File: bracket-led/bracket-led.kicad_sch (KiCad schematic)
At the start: 1 part, among them J1 BM08B-SURS-TF(LF)(SN)

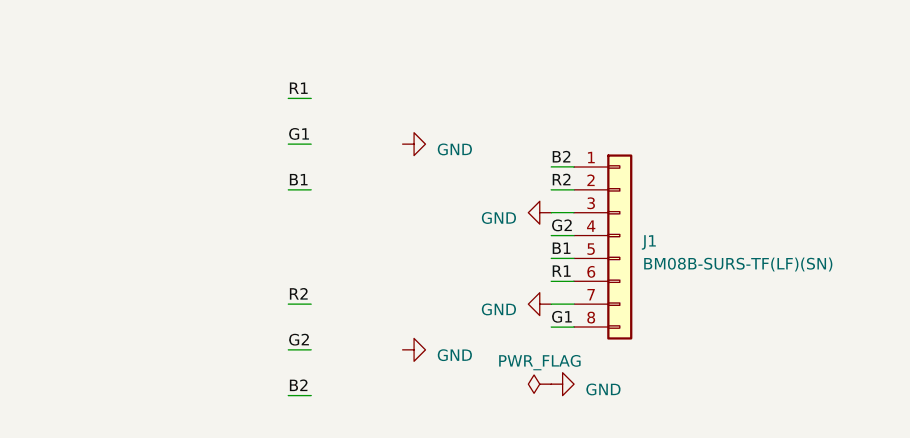
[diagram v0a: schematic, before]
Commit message: LED PCB perpendicular to bracket
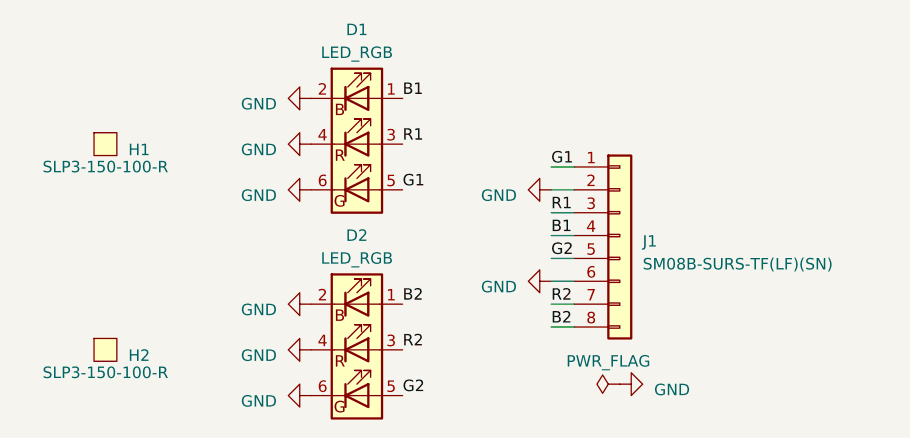
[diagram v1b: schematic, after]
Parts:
- added D1, D2: LED_RGB, Open Ephys:EVERLIGHT_6-SMD-1.6x1.6, symbol Open Ephys:EAST1616RGBA8
- added H1, H2: SLP3-150-100-R, Open Ephys: SLP3-150-100-R, symbol Open Ephys:SLP3-150-100-R
- J1: value BM08B-SURS-TF(LF)(SN) -> SM08B-SURS-TF(LF)(SN); footprint jonnew:JST_BM08B-SURS-TF(LF)(SN) -> Open Ephys:JST_SM08B-SURS-TF(LF)(SN)
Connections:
- net B1: now also J1.4 (Pin_4), D1.1 (BA); no longer J1.5 (Pin_5)
- net B2: now also J1.8 (Pin_8), D2.1 (BA); no longer J1.1 (Pin_1)
- net G1: now also J1.1 (Pin_1), D1.5 (GA); no longer J1.8 (Pin_8)
- net G2: now also J1.5 (Pin_5), D2.5 (GA); no longer J1.4 (Pin_4)
- net GND: now also J1.2 (Pin_2), J1.6 (Pin_6), D1.2 (BK), D1.4 (RK), D1.6 (GK), D2.2 (BK), D2.4 (RK), D2.6 (GK); no longer J1.3 (Pin_3), J1.7 (Pin_7)
- net R1: now also J1.3 (Pin_3), D1.3 (RA); no longer J1.6 (Pin_6)
- net R2: now also J1.7 (Pin_7), D2.3 (RA); no longer J1.2 (Pin_2)
